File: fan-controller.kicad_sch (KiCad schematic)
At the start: 14 parts, among them J1 PWR, J2 PTC, J3 FAN, J4 Prog, Q1 AO3401A, U1 PY32F002A

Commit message: Fix ERC
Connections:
- no-connect marks 0 -> 1
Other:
- moved on the sheet: J1

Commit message: Final touch-ups
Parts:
- removed C2: 10u, Resistor_SMD:R_1206_3216Metric, symbol Device:C
- removed D1: ZMM3V3-M, Diode_SMD:D_MiniMELF, symbol Device:D_Zener
- removed J4: Prog, Connector_PinHeader_2.54mm:PinHeader_1x04_P2.54mm_Vertical, symbol Connector_Generic:Conn_01x04
- removed R1: 10k, Resistor_SMD:R_0603_1608Metric, symbol Device:R
- added C4: 10u, Resistor_SMD:R_1206_3216Metric, symbol Device:C
- added J4: Conn_ARM_SWD_TagConnect_TC2030-NL, Connector:Tag-Connect_TC2030-IDC-NL_2x03_P1.27mm_Vertical, symbol Connector:Conn_ARM_SWD_TagConnect_TC2030-NL
- added U2: L78L05, Package_TO_SOT_SMD:SOT-89-3, symbol Regulator_Linear:L78L05_SOT89
- U1: LCSC C5128435 -> C5292060
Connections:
- net +3.3V: now also J4.1 (VCC), U2.1 (OUT)
- net GND: now also C4.2, J4.5 (GND), U2.2 (GND)
- net SWCLK: now also J4.2 (SWDIO)
- net SWDIO: now also J4.4 (SWCLK)
- net VPP: now also C4.1, U2.3 (IN)
- no-connect marks 1 -> 3
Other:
- moved on the sheet: C1, J1

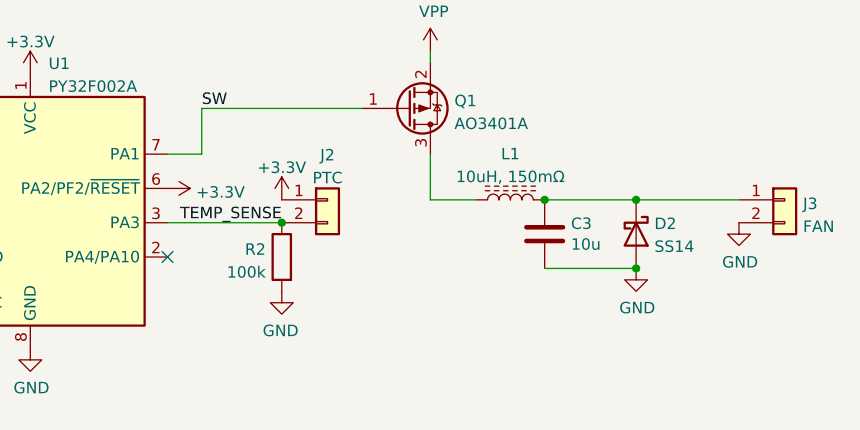
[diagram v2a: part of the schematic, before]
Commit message: Fix flyback diode & add output sense
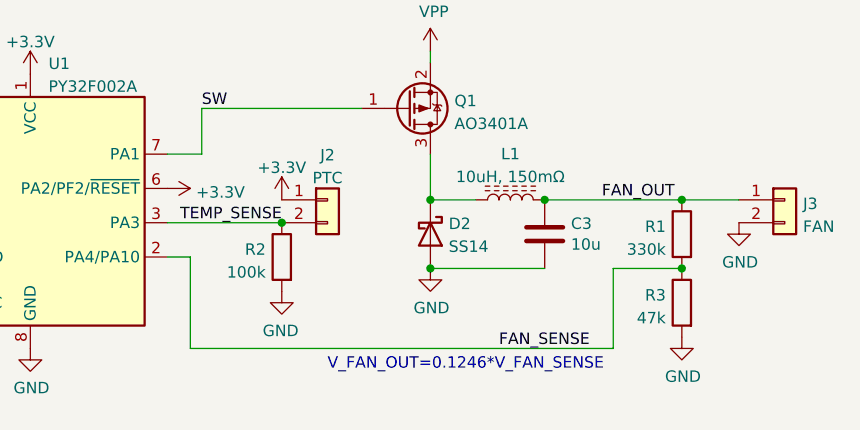
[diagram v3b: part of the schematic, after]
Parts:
- added R1: 330k, Resistor_SMD:R_0603_1608Metric, symbol Device:R
- added R3: 47k, Resistor_SMD:R_0603_1608Metric, symbol Device:R
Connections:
- net GND: now also R3.2
- net at L1.1, Q1.3 (D): now also D2.1 (K)
- net FAN_OUT: now reaches C3.1, J3.1 (Pin_1), L1.2
- net FAN_OUT: now also R1.1; no longer D2.1 (K)
- net FAN_SENSE: now reaches U1.2 (PA4/PA10)
- net FAN_SENSE: now also R1.2, R3.1
- no-connect marks 3 -> 2
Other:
- note added: "V_FAN_OUT=0.1246*V_FAN_SENSE"
- moved on the sheet: D2
